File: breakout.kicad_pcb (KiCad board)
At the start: 2 copper layers, 114.8 x 122.8 mm, 32 parts, among them CON1 SD_Card, CON2 USB-MICRO-AB, P2 CONN_01X40, P3 CONN_01X40, P4 CONN_01X40, P5 A-DF-09-A/KG-T4S

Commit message: removed unecessary fuse, checked footprints
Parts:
- removed F1: 0603SFV300F/32-2, SMD_Packages:SMD-1206_Pol
- removed GND1: CONN_01X02, Terminal_Blocks:TerminalBlock_WAGO-236_2Stift_RM5mm_1pol
- added SW1: SW_PUSH, Custom Footprints:1825910-7, F.Cu at (126.2, 197.3)
- C1: footprint Capacitors_SMD:C_0201 -> Capacitors_Elko_ThroughHole:Elko_vert_25x12.5mm_RM5_CopperClear
- C2: footprint Capacitors_SMD:C_0201 -> Capacitors_Tantalum_SMD:TantalC_SizeB_EIA-3528_Reflow
- C3: footprint Capacitors_SMD:C_0402 -> Capacitors_Tantalum_SMD:TantalC_SizeC_EIA-6032_Reflow
- C5, C6: footprint Capacitors_SMD:C_0402 -> Capacitors_SMD:C_0805
- D1: value D_Small -> B340; footprint Diodes_ThroughHole:Diode_DO-35_SOD27_Horizontal_RM10 -> Diodes_SMD:Diode-SMC_Standard
- L1: footprint SMD_Packages:SMD-1206_Pol -> Choke_SMD:Choke_SMD_12x12mm_h8mm
- L2: footprint Capacitors_SMD:C_0201 -> Capacitors_SMD:C_0805
- POWER1: footprint Terminal_Blocks:TerminalBlock_WAGO-236_2Stift_RM5mm_1pol -> Custom Footprints:1792863
- moved C1 31.3 mm to (95.2, 144.9), turned to 270 degrees
- moved C2 16.6 mm to (105.1, 193.8)
- moved L1 15.9 mm to (117.0, 192.9)
- moved C3 11.0 mm to (108.7, 139.8)
- moved POWER1 6.22 mm to (96.9, 180.9), turned to 270 degrees
- moved G1 6.08 mm to (145.8, 205.5)
- moved D1 2.59 mm to (110.1, 181.4)
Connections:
- C1 pad 1: Net-(C1-Pad1) -> /RAIL
- PWR1 pad 1: Net-(C1-Pad1) -> /RAIL
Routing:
- net GND: track 12.6 -> 1.40 mm
- net Net-(C1-Pad1): track 9.12 -> 0.00 mm
- net /3.3V: track 5.01 -> 0.00 mm
- net /RAIL: track 5.00 -> 0.00 mm
- net Net-(D1-Pad2): track 6.23 -> 1.25 mm

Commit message: added battery to schematic
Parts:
- added B1: BS-5, Custom Footprints:BS-5, F.Cu at (102.4, 127.5)
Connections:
- CPU1 pad 127: /3.3V -> /BAT3.0V
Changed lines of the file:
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@@
 (kicad_pcb (version 4) (host pcbnew "(after 2015-mar-04 BZR unknown)-product")
   (general
-    (links 116)
-    (no_connects 114)
-    (area 65.862999 107.391999 180.771001 230.301001)
+    (links 118)
+    (no_connects 116)
+    (area 65.862999 107.391999 183.468334 263.457109)
     (thickness 1.6)
     (drawings 6)
     (tracks 5)
     (zones 0)
-    (modules 31)
-    (nets 34)
+    (modules 32)
+    (nets 35)
   )
   (page USLetter portrait)
@@
   (net 32 "Net-(CON1-Pad12)")
   (net 33 /RESET)
+  (net 34 /BAT3.0V)
   (net_class Default "This is the default net class."
     (clearance 0.2)
@@
     (add_net /3.3V)
     (add_net /5V)
+    (add_net /BAT3.0V)
     (add_net /IC_WP)
     (add_net /ISP_ENABLE)
@@
     (pad 126 smd rect (at 0.25 -10.7 90) (size 1.55 0.3) (layers F.Cu F.Paste F.Mask))
     (pad 127 smd rect (at -0.25 -10.7 90) (size 1.55 0.3) (layers F.Cu F.Paste F.Mask)
-      (net 8 /3.3V))
+      (net 34 /BAT3.0V))
     (pad 128 smd rect (at -0.75 -10.7 90) (size 1.55 0.3) (layers F.Cu F.Paste F.Mask)
       (net 33 /RESET))
@@
     )
   )
+  (module "Custom Footprints:BS-5" (layer F.Cu)
+    (at 102.4128 127.4826 180)
+    (fp_text reference B1 (at 0 -2 180) (layer F.SilkS)
+      (effects (font (size 1 1) (thickness 0.15)))
+    )
+    (fp_text value BS-5 (at 0 0 180) (layer F.Fab)
+      (effects (font (size 1 1) (thickness 0.15)))
+    )
+    (fp_line (start 7 -5) (end -7 -5) (layer F.SilkS) (width 0.15))
+    (fp_line (start 7 1) (end -7 1) (layer F.SilkS) (width 0.15))
+    (fp_line (start -1.25 -3.75) (end -2.25 -3.75) (layer F.SilkS) (width 0.15))
+    (fp_line (start 2.75 0) (end 3.75 0) (layer F.SilkS) (width 0.15))
+    (fp_line (start 3.25 0.5) (end 3.25 -0.5) (layer F.SilkS) (width 0.15))
+    (fp_line (start 7 1) (end 7 -5) (layer F.SilkS) (width 0.15))
+    (fp_line (start -7 1) (end -7 -5) (layer F.SilkS) (width 0.15))
+    (fp_line (start -12 1) (end -12 -5) (layer Cmts.User) (width 0.15))
+    (fp_line (start 12 1) (end 12 -5) (layer Cmts.User) (width 0.15))
+    (fp_line (start 12 -5) (end -12 -5) (layer Cmts.User) (width 0.15))
+    (fp_line (start -12 1) (end 12 1) (layer Cmts.User) (width 0.15))
+    (pad 1 thru_hole circle (at -5 0 180) (size 1 1) (drill 0.6) (layers *.Cu *.Mask F.SilkS)
+      (net 34 /BAT3.0V))
+    (pad 2 thru_hole circle (at 0 -3.81 180) (size 1 1) (drill 0.6) (layers *.Cu *.Mask F.SilkS)
+      (net 1 GND))
+    (pad 1 thru_hole circle (at 5 0 180) (size 1 1) (drill 0.6) (layers *.Cu *.Mask F.SilkS)
+      (net 34 /BAT3.0V))
+  )
   (gr_line (start 65.913 230.251) (end 65.913 107.442) (angle 90) (layer Edge.Cuts) (width 0.1))

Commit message: cleaned out old traces, and set minimum track widths
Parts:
- moved D1 10.3 mm to (119.9, 178.5)
- moved P4 3.41 mm to (171.9, 127.5)
- moved POWER1 2.93 mm to (96.6, 178.0)
- moved P3 2.43 mm to (163.3, 124.6)
- moved PWR2 0.79 mm to (124.0, 155.8)
- moved PWR1 0.54 mm to (108.6, 176.3)
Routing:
- net GND: track 1.40 -> 0.00 mm
- net Net-(D1-Pad2): track 1.25 -> 0.00 mm
- removed copper zone on F.Cu, net GND
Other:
- net class Default: clearance 0.2 -> 0.254; trace_width 0.25 -> 0.254
- rule trace_clearance: 0.2 -> 0.254
- rule trace_min: 0.2 -> 0.254
- rule via_min_drill: 0.3 -> 0.4
- rule via_min_size: 0.4 -> 0.42
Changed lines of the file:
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@@
     (links 118)
     (no_connects 116)
-    (area 65.862999 107.391999 183.468334 263.457109)
+    (area 65.862999 107.391999 180.771001 230.301001)
     (thickness 1.6)
     (drawings 6)
-    (tracks 5)
+    (tracks 2)
     (zones 0)
     (modules 32)
@@
   )
   (setup
-    (last_trace_width 0.25)
-    (trace_clearance 0.2)
+    (last_trace_width 0.254)
+    (trace_clearance 0.254)
     (zone_clearance 0.508)
     (zone_45_only yes)
-    (trace_min 0.2)
+    (trace_min 0.254)
     (segment_width 0.2)
     (edge_width 0.1)
     (via_size 0.6)
     (via_drill 0.4)
-    (via_min_size 0.4)
-    (via_min_drill 0.3)
+    (via_min_size 0.42)
+    (via_min_drill 0.4)
     (uvia_size 0.3)
     (uvia_drill 0.1)
@@
   (net 34 /BAT3.0V)
   (net_class Default "This is the default net class."
-    (clearance 0.2)
-    (trace_width 0.25)
+    (clearance 0.254)
+    (trace_width 0.254)
     (via_dia 0.6)
     (via_drill 0.4)
@@
   )
   (module Socket_Strips:Socket_Strip_Straight_1x40 (layer F.Cu)
-    (at 161.163 125.73 270)
+    (at 163.2966 124.5616 270)
     (descr "Through hole socket strip")
     (tags "socket strip")
@@
   )
   (module Socket_Strips:Socket_Strip_Straight_1x40 (layer F.Cu)
-    (at 175.26 128.2192 270)
+    (at 171.9326 127.4826 270)
     (descr "Through hole socket strip")
     (tags "socket strip")
@@
   )
   (module SMD_Packages:TO-263-5 (layer F.Cu)
-    (at 109.093 176.149)
+    (at 108.585 176.3268)
     (attr smd)
     (fp_text reference PWR1 (at 0 -5.969) (layer F.SilkS)
@@
   )
   (module Housings_DFN_QFN:QFN-16-1EP_3x3mm_Pitch0.5mm (layer F.Cu)
-    (at 123.19 155.829)
+    (at 123.9774 155.8036)
     (descr "16-Lead Plastic Quad Flat, No Lead Package (NG) - 3x3x0.9 mm Body [QFN]; (see Microchip Packaging Specification 00000049BS.pdf)")
     (tags "QFN 0.5")
@@
   )
   (module Diodes_SMD:Diode-SMC_Standard (layer F.Cu)
-    (at 110.0836 181.3814 180)
+    (at 119.9388 178.4604 180)
     (descr "Diode SMC Standard")
     (tags "Diode SMC Standard")
@@
   )
   (module "Custom Footprints:1792863" (layer F.Cu)
-    (at 96.8502 180.9496 270)
+    (at 96.5962 178.0286 270)
     (tags "CONN TERM BLOCK 5MM 2POS GRN")
     (fp_text reference POWER1 (at -3.7592 0.508 360) (layer F.SilkS)
@@
   )
   (gr_circle (center 88.519 258.064) (end 90.297 262.89) (layer F.SilkS) (width 0.5))
-  (segment (start 112.49406 180.3908) (end 113.48466 181.3814) (width 0.25) (layer F.Cu) (net 1))
-  (segment (start 107.39374 180.6702) (end 106.68254 181.3814) (width 0.25) (layer F.Cu) (net 6))
-  (segment (start 107.39374 176.149) (end 107.569 176.32426) (width 0.25) (layer F.Cu) (net 6))
   (via (at 97.536 211.939) (size 0.6) (layers F.Cu B.Cu) (net 9) (status 30))
   (segment (start 97.536 209.169) (end 97.79 209.169) (width 0.25) (layer F.Cu) (net 10) (status 30))
-  (zone (net 1) (net_name GND) (layer F.Cu) (hatch edge 0.508)
-    (connect_pads yes (clearance 0.508))
-    (min_thickness 0.254)
-    (fill yes (arc_segments 16) (thermal_gap 0.508) (thermal_bridge_width 0.508))
-    (polygon
-      (pts
-        (xy 115.316 173.99) (xy 112.903 173.99) (xy 112.903 175.133) (xy 112.014 175.133) (xy 112.014 173.99)
-        (xy 109.601 173.99) (xy 109.601 175.133) (xy 108.585 175.133) (xy 108.585 173.99) (xy 93.091 173.99)
-        (xy 93.091 160.02) (xy 115.316 160.02)
-      )
-    )
-  )
 )

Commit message: starting shuffle and board trace
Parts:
- moved P2 101.5 mm to (162.1, 122.7), turned to 270 degrees
- moved SW1 44.0 mm to (82.3, 201.3), turned to 90 degrees
- moved G1 43.8 mm to (103.6, 217.0), turned to 0 degrees
- moved CPU1 34.8 mm to (113.7, 198.0), turned to 90 degrees
- moved S1 34.4 mm to (129.2, 183.0), turned to 0 degrees
- moved POWER1 34.0 mm to (92.4, 144.3)
- moved L1 27.7 mm to (124.1, 166.2)
- moved CON2 25.8 mm to (120.2, 215.1)
- moved CON1 15.4 mm to (131.0, 200.2), turned to 90 degrees
- moved C1 14.3 mm to (96.6, 159.1), turned to 180 degrees
- moved C2 13.3 mm to (110.5, 181.6), turned to 180 degrees
- moved P5 10.7 mm to (92.6, 199.1)
- moved PWR1 6.57 mm to (103.8, 171.8), turned to 90 degrees
- moved P3 6.02 mm to (169.3, 124.2)
- moved P4 4.10 mm to (174.3, 124.2)
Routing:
- net (no net): track 0.00 -> 0.25 mm, vias 0 -> 1
- net Net-(CPU1-Pad75): vias 1 -> 0

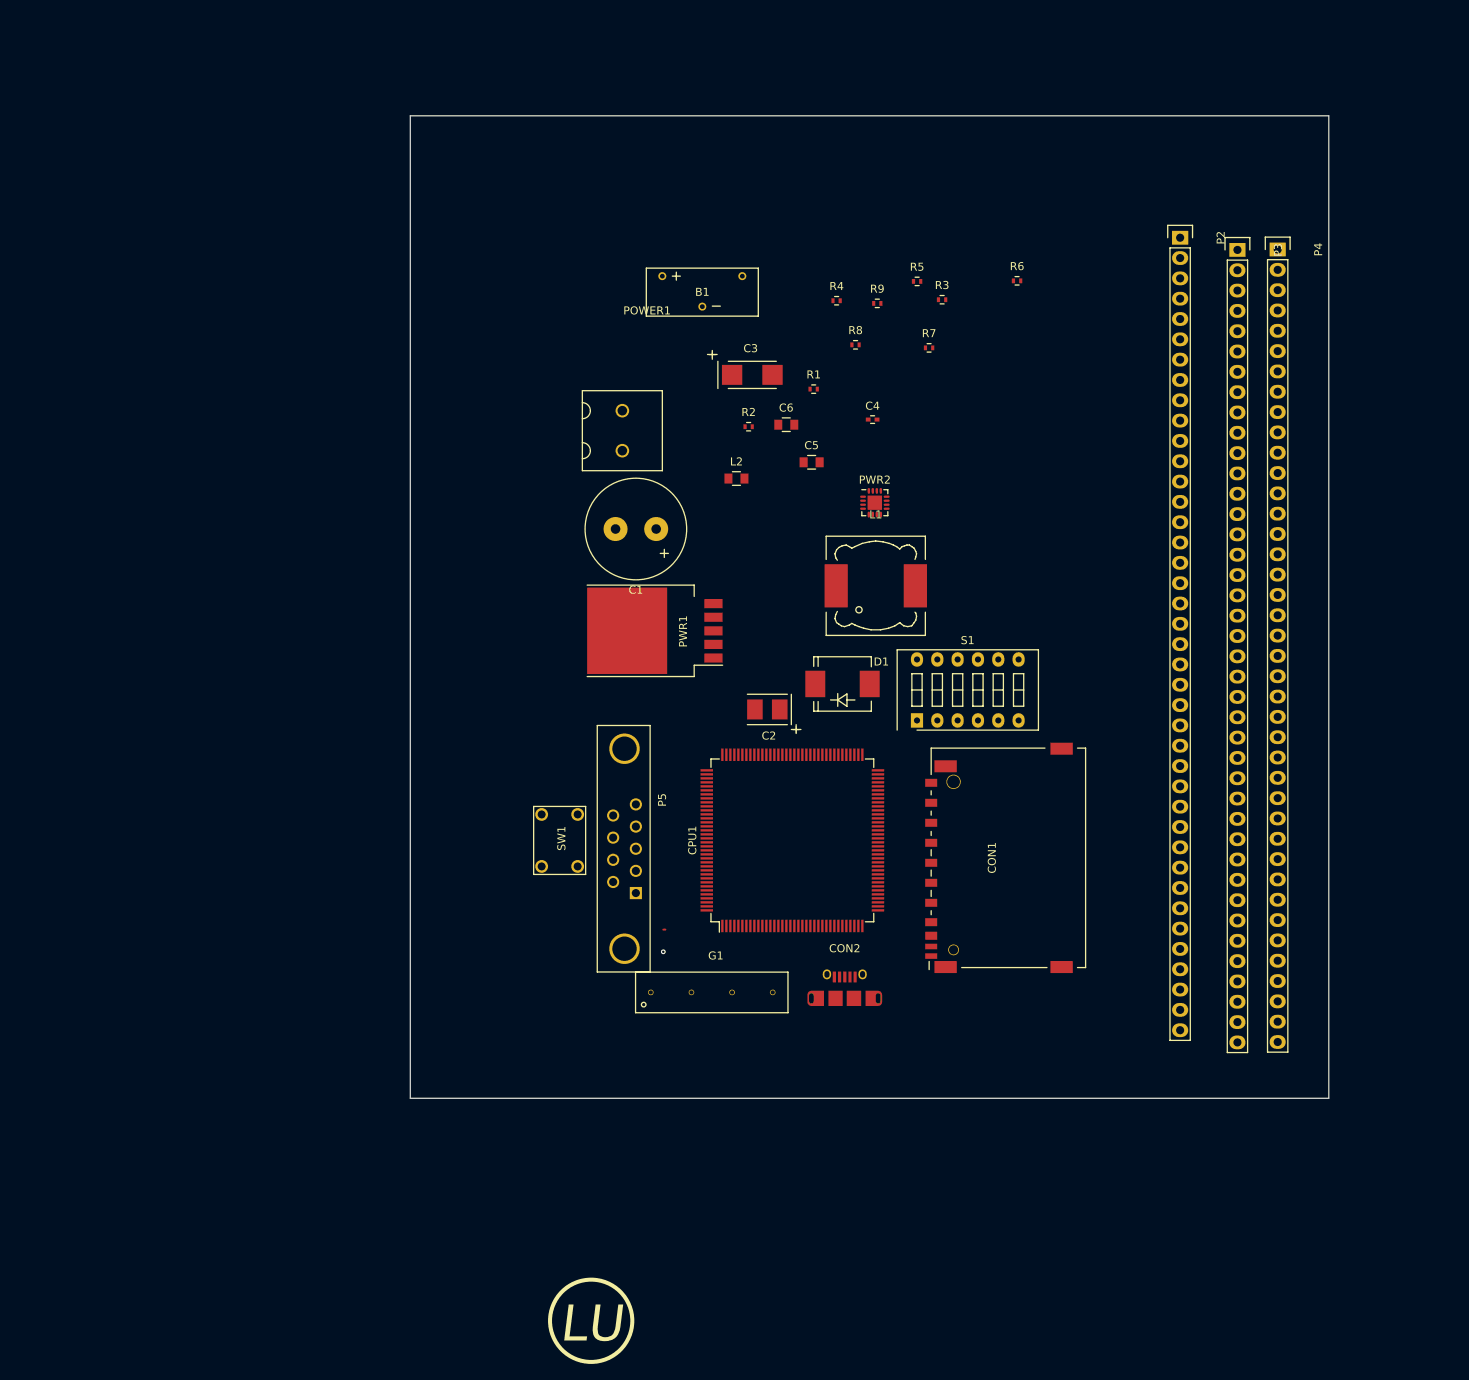
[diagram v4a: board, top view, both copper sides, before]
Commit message: PCB: separated components and grouped by function
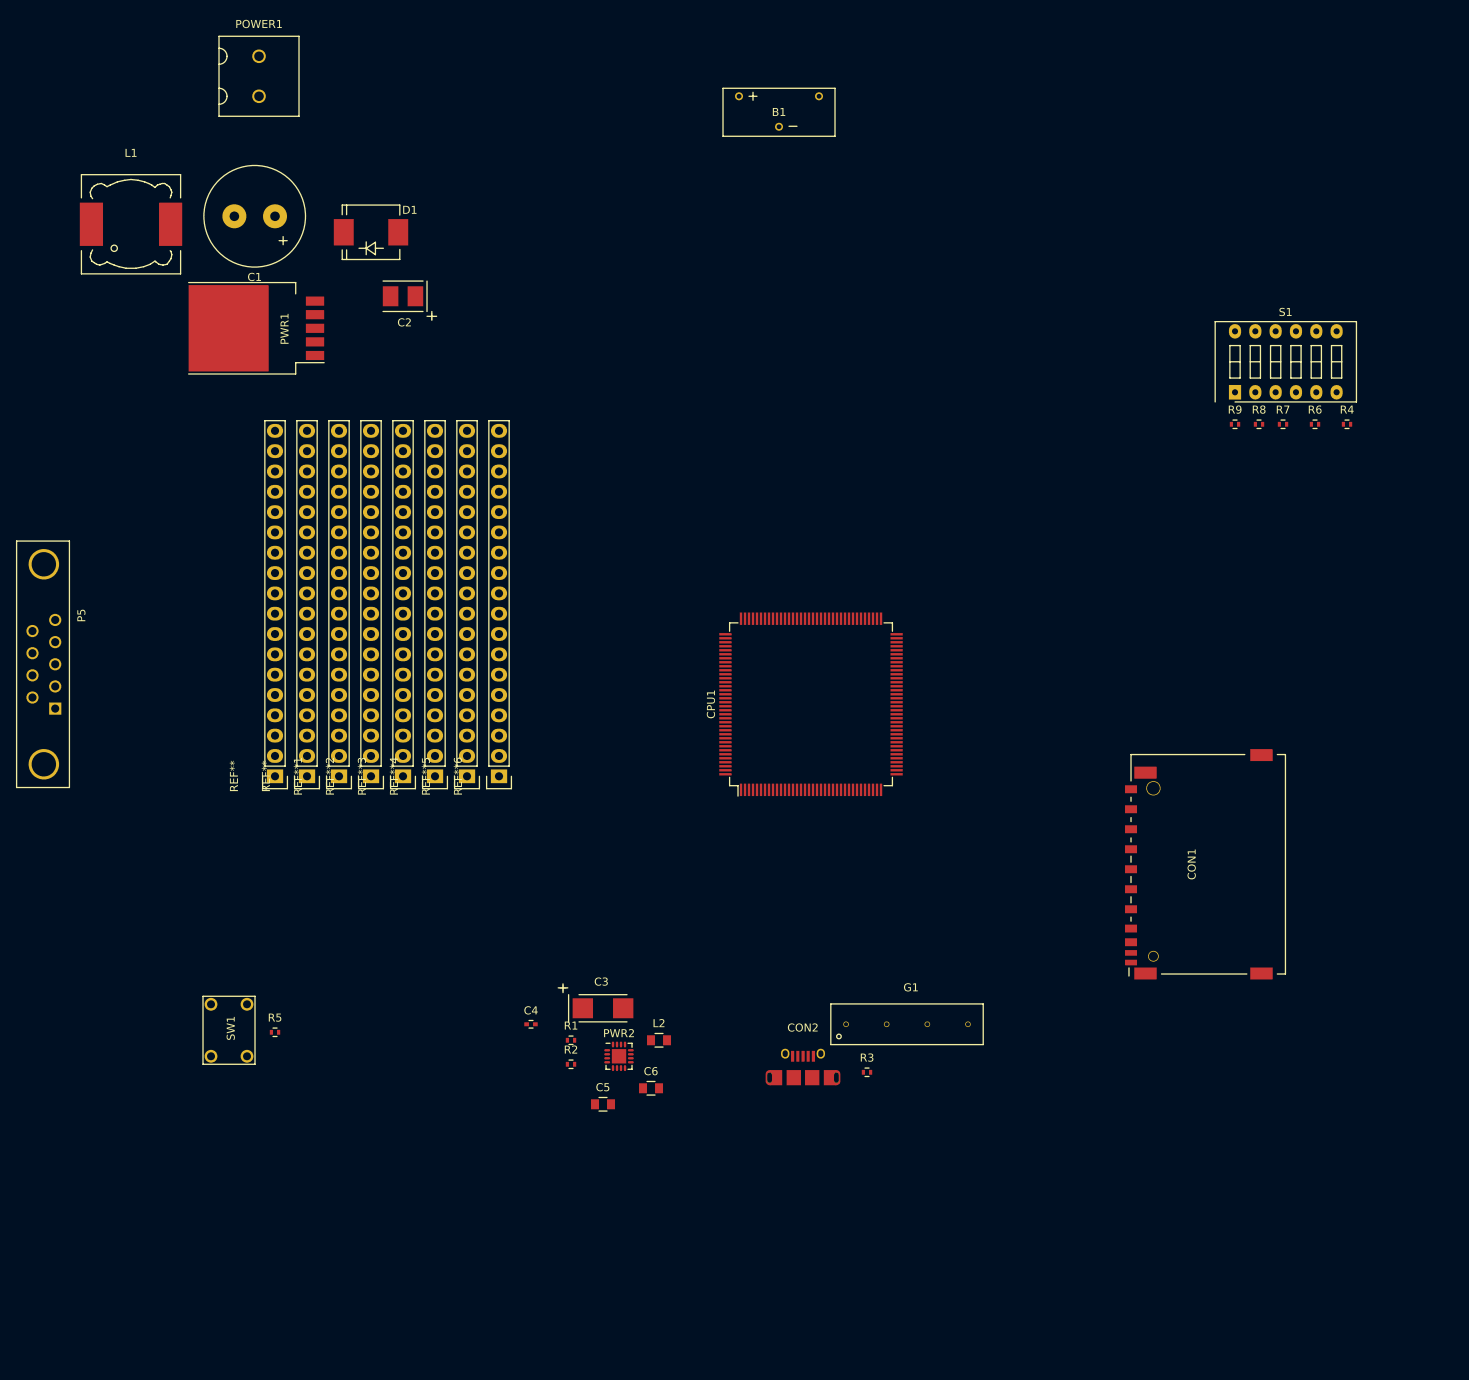
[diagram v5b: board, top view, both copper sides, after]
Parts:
- removed P2, P3, P4: CONN_01X40, Socket_Strips:Socket_Strip_Straight_1x40
- added REF**: Socket_Strip_Straight_1x18, Socket_Strips:Socket_Strip_Straight_1x18, F.Cu at (53.0, 190.0)
- added REF**: Socket_Strip_Straight_1x18, Socket_Strips:Socket_Strip_Straight_1x18, F.Cu at (49.0, 190.0)
- added REF**1: Socket_Strip_Straight_1x18, Socket_Strips:Socket_Strip_Straight_1x18, F.Cu at (57.0, 190.0)
- added REF**2: Socket_Strip_Straight_1x18, Socket_Strips:Socket_Strip_Straight_1x18, F.Cu at (61.0, 190.0)
- added REF**3: Socket_Strip_Straight_1x18, Socket_Strips:Socket_Strip_Straight_1x18, F.Cu at (65.0, 190.0)
- added REF**4: Socket_Strip_Straight_1x18, Socket_Strips:Socket_Strip_Straight_1x18, F.Cu at (69.0, 190.0)
- added REF**5: Socket_Strip_Straight_1x18, Socket_Strips:Socket_Strip_Straight_1x18, F.Cu at (73.0, 190.0)
- added REF**6: Socket_Strip_Straight_1x18, Socket_Strips:Socket_Strip_Straight_1x18, F.Cu at (77.0, 190.0)
- moved R5 123.5 mm to (49.0, 222.0)
- moved L1 103.5 mm to (31.0, 121.0)
- moved R3 97.0 mm to (123.0, 227.0)
- moved R1 86.9 mm to (86.0, 223.0)
- moved C4 86.8 mm to (81.0, 221.0)
- moved C6 84.7 mm to (96.0, 229.0)
- moved C5 84.4 mm to (90.0, 231.0)
- moved R2 82.7 mm to (86.0, 226.0)
- moved D1 81.6 mm to (61.0, 122.0)
- moved C3 81.3 mm to (90.0, 219.0)
- moved PWR2 76.2 mm to (92.0, 225.0)
- moved P5 76.2 mm to (20.0, 176.0)
- moved L2 70.9 mm to (97.0, 223.0)
- moved C2 68.9 mm to (65.0, 130.0)
- moved R4 65.6 mm to (183.0, 146.0)
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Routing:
- net (no net): track 0.25 -> 0.00 mm, vias 1 -> 0
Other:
- board outline removed
- board text removed: "LU"

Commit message: set the design rules
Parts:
- moved P5 107.9 mm to (121.0, 138.0), turned to 180 degrees
- moved REF**5 79.1 mm to (140.0, 148.0), turned to 180 degrees
- moved REF**6 78.0 mm to (140.0, 144.0), turned to 180 degrees
- moved B1 75.4 mm to (84.0, 175.0)
- moved CON2 27.1 mm to (117.0, 198.0)
- moved C3 13.0 mm to (101.0, 212.0)
- moved C4 13.0 mm to (92.0, 214.0)
- moved C5 13.0 mm to (101.0, 224.0)
- moved C6 13.0 mm to (107.0, 222.0)
- moved L2 13.0 mm to (108.0, 216.0)
- moved PWR2 13.0 mm to (103.0, 218.0)
- moved R1 13.0 mm to (97.0, 216.0)
- moved R2 13.0 mm to (97.0, 219.0)
- moved CPU1 0.52 mm to (116.2, 180.5)
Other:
- net class 0.3mm added: clearance 0.0762, trace_width 0.3, via_dia 0.4318, via_drill 0.381
- net class Default: clearance 0.254 -> 0.0762; trace_width 0.254 -> 0.1524; via_dia 0.6 -> 0.4318; via_drill 0.4 -> 0.381
- rule trace_clearance: 0.254 -> 0.0762
- rule trace_min: 0.254 -> 0.1524
- rule via_min_drill: 0.4 -> 0.1016
- rule via_min_size: 0.42 -> 0.127

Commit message: fixing net names
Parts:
- removed REF** (x2), REF**1, REF**2, REF**3, REF**4, REF**5, REF**6: Socket_Strip_Straight_1x18, Socket_Strips:Socket_Strip_Straight_1x18
- added P2: CONN_01X40, Socket_Strips:Socket_Strip_Straight_1x40, F.Cu at (84.3, 157.3)
- added P3: CONN_01X40, Socket_Strips:Socket_Strip_Straight_1x40, F.Cu at (84.5, 152.5)
- added P4: CONN_01X40, Socket_Strips:Socket_Strip_Straight_1x40, F.Cu at (84.3, 161.6)
